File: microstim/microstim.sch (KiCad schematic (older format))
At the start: 81 parts

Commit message: tons of updates - beginning of layout as well.
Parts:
- removed BT?: 9V, symbol Device:Battery_Cell
- removed C? (x2): 1uF, symbol Device:C_Small
- removed U?: MCP3002, symbol Analog_ADC:MCP3002
- removed U?: L79L05_SO8, Package_SO:SOIC-8_3.9x4.9mm_P1.27mm, symbol Regulator_Linear:L79L05_SO8
- removed U? (x2): FQP47P06, symbol natecermak:FQP47P06
- removed U?: DG4053, symbol natecermak:DG4053
- added C11, C13, C16, C17, C37, C38, C39, C41, C5: 0.1uF, Capacitor_SMD:C_0603_1608Metric, symbol Device:C_Small
- added C28, C29: 100pF, Capacitor_SMD:C_0603_1608Metric, symbol Device:C_Small
- added C42: 680nF, Capacitor_SMD:C_0603_1608Metric, symbol Device:C_Small
- added R13, R14: 1k, Resistor_SMD:R_0603_1608Metric, symbol Device:R_US
- added RV4: 1k, Potentiometer_THT:Potentiometer_Bourns_3296Y_Vertical, symbol Device:R_POT
- added U10: AD7321, Package_SO:TSSOP-14_4.4x5mm_P0.65mm, symbol natecermak:AD7321
- added U17: LM358, Package_SO:SOIC-8_3.9x4.9mm_P1.27mm, symbol Amplifier_Operational:LM358
- added U18, U19: DG509ACWE, Package_SO:SOIC-16_3.9x9.9mm_P1.27mm, symbol natecermak:DG509ACWE
- added U7: ISO7341C, Package_SO:SOIC-16W_7.5x10.3mm_P1.27mm, symbol Isolator:ISO7341C
- C1, C10, C12, C14, C15, C18, C19, C2, C20, C21, C22, C23, C24, C25, C26, C27, C3, C30, C31, C32, C33, C34, C35, C36, C4, C40, C6, C7, C8, C9: renamed from C?; footprint (none) -> Capacitor_SMD:C_0603_1608Metric
- J1, J10, J12, J2, J5, J6: renamed from J?; footprint (none) -> Connector_Coaxial:SMA_Amphenol_901-144_Vertical
- J11: renamed from J?; footprint (none) -> TerminalBlock_4Ucon:TerminalBlock_4Ucon_1x02_P3.50mm_Horizontal
- J3, J4, J7, J8, J9: renamed from J?; footprint (none) -> TerminalBlock_4Ucon:TerminalBlock_4Ucon_1x02_P3.50mm_Vertical
- R1, R10, R11, R12, R2, R3, R4, R5, R6, R7, R8, R9: renamed from R?; footprint (none) -> Resistor_SMD:R_0603_1608Metric
- RV1, RV2, RV3: renamed from RV?; footprint (none) -> Potentiometer_THT:Potentiometer_Bourns_3296Y_Vertical
- SW1, SW2: renamed from SW?; footprint (none) -> Button_Switch_THT:SW_PUSH_6mm
- U1: renamed from U?; footprint (none) -> microstim:Teensy35_36
- U11, U12: renamed from U?; footprint (none) -> Package_SO:SOIC-8-N7_3.9x4.9mm_P1.27mm
- U13, U14: renamed from U?; footprint 21-0042B_16 -> Package_SO:SOIC-16_3.9x9.9mm_P1.27mm
- U15, U16: renamed from U?; footprint (none) -> Package_SO:SOIC-8_3.9x4.9mm_P1.27mm
- U2: renamed from U?; footprint (none) -> microstim:CC3-0512DF-E
- U9: renamed from U?; footprint (none) -> Package_SO:SOIC-14_3.9x8.7mm_P1.27mm
- gave numbers to parts that had none: 5
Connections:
- net labels added: CS2, CS2i, ISENSE0, ISENSE1, MISO2, MISO2i, MOSI2, MOSI2i, SCK2, SCK2i
- net labels removed: -5V, VIN_TEENSY
- wire segments 384 -> 497
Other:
- moved on the sheet: C1, C10, C12, C14, C15, C18, C19, C2, C20, C21, C22, C23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

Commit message: first complete draft of microstim PCB. no errors in layout.
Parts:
- removed U11, U12: LTC2057, Package_SO:SOIC-8-N7_3.9x4.9mm_P1.27mm, symbol natecermak:LTC2057
- added U11, U12: LTC2057, Package_SO:SOIC-8_3.9x4.9mm_P1.27mm, symbol Linear_Technology:LTC2057
- J11: footprint TerminalBlock_4Ucon:TerminalBlock_4Ucon_1x02_P3.50mm_Horizontal -> TerminalBlock_4Ucon:TerminalBlock_4Ucon_1x02_P3.50mm_Vertical
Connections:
- wire segments 497 -> 504
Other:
- moved on the sheet: RV1, RV4, SW1, SW2

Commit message: fixed some op-amps inserted backwards. also had to recommit everything due to OS upgrade and HD backup.
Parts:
- removed U11, U12: LTC2057, Package_SO:SOIC-8_3.9x4.9mm_P1.27mm, symbol Linear_Technology:LTC2057
- added U11, U12: LTC2057, Package_SO:SOIC-8-N7_3.9x4.9mm_P1.27mm, symbol natecermak:LTC2057
- C1: footprint Capacitor_SMD:C_0603_1608Metric -> Capacitor_SMD:C_1206_3216Metric_Pad1.42x1.75mm_HandSolder
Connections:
- wire segments 504 -> 509
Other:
- moved on the sheet: C21, C23, C26

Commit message: redesign based on improved howland source at jon newmans suggestion
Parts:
- removed C10, C26, C27, C30, C32, C34, C35, C37, C38, C39, C4, C41: 0.1uF, Capacitor_SMD:C_0603_1608Metric, symbol Device:C_Small
- removed C28, C29: 100pF, Capacitor_SMD:C_0603_1608Metric, symbol Device:C_Small
- removed R10: 5.5k, Resistor_SMD:R_0603_1608Metric, symbol Device:R_US
- removed R11, R12: 50k, Resistor_SMD:R_0603_1608Metric, symbol Device:R_US
- removed R14: 1k, Resistor_SMD:R_0603_1608Metric, symbol Device:R_US
- removed RV2, RV3: 1k, Potentiometer_THT:Potentiometer_Bourns_3296Y_Vertical, symbol Device:R_POT
- removed U11, U12: LTC2057, Package_SO:SOIC-8-N7_3.9x4.9mm_P1.27mm, symbol natecermak:LTC2057
- removed U13, U14, U19: DG509ACWE, Package_SO:SOIC-16_3.9x9.9mm_P1.27mm, symbol natecermak:DG509ACWE
- removed U16: LT1167, Package_SO:SOIC-8_3.9x4.9mm_P1.27mm, symbol natecermak:LT1167
- removed U17: LM358, Package_SO:SOIC-8_3.9x4.9mm_P1.27mm, symbol Amplifier_Operational:LM358
- removed U6: ISO7760, Package_SO:SOIC-16W_7.5x10.3mm_P1.27mm, symbol natecermak:ISO7760
- added U11: LT6657AHMS8-2.5, Package_SO:MSOP-8_3x3mm_P0.65mm, symbol Reference_Voltage:LT6657AHMS8-2.5
- added U12, U13: AD8276, Package_SO:SOIC-8_3.9x4.9mm_P1.27mm, symbol Amplifier_Difference:AD8276
- added U14: LT1167, Package_SO:SOIC-8_3.9x4.9mm_P1.27mm, symbol natecermak:LT1167
- added U16: DG509ACWE, Package_SO:SOIC-16_3.9x9.9mm_P1.27mm, symbol natecermak:DG509ACWE
- R1, R2, R5: value 25k -> 3k
- R4: value 250 -> 3k
- R6: value 25k -> 250
- R7: value 1k -> 1.2k
- R8: value 5.5k -> 1.2k
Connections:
- net labels added: 2.5V
- net labels removed: GS0_0, GS0_0i, GS0_1, GS0_1i, GS1_0, GS1_0i, GS1_1, GS1_1i
- wire segments 509 -> 365
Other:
- note added: "Max current output (0ohm load) is 2.5V/3k = +- 833uA.\nCurrent resolution is 5V/4096/3k = 0.4uA\nMax voltage output (infinite load) is 40/43*12V = 11.16V"
- note added: "gain is Rsense*(1+49.4k/Rg) = 250*(1+49.4k/1.2k) = 10.5 mV/uA\nVoltage output range is thus +-833*0.0105 = +-8.7V\noutput needs to be within +-10V\n"
- moved on the sheet: C12, C14, C20, C21, C31, C33, C36, C40, J1, J10, J11, J12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

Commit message: lots of cleanup in file structure. nearly ready to order board v0.12. need to finish BOM and commit.
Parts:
- removed U11: LT6657AHMS8-2.5, Package_SO:MSOP-8_3x3mm_P0.65mm, symbol Reference_Voltage:LT6657AHMS8-2.5
- added C4: 1uF, Capacitor_SMD:C_0603_1608Metric, symbol Device:C_Small
- added U6: AD1582, Package_TO_SOT_SMD:SOT-23, symbol natecermak:AD1582
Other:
- moved on the sheet: C1, C11, C12, C13, C14, C15, C16, C17, C18, C19, C2, C20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

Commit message: replaced LT1167 with INA826 instrument amp. hopefully this wasn't a terrible decision.
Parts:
- removed U14, U15: LT1167, Package_SO:SOIC-8_3.9x4.9mm_P1.27mm, symbol natecermak:LT1167
- added U11, U14: INA826, Package_SO:SOIC-8_3.9x4.9mm_P1.27mm, symbol natecermak:INA826
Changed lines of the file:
@@
 	6550 3950 6350 3950
-$Comp
-L natecermak:LT1167 U15
-U 1 1 5B7A1A5B
-P 11400 1050
-F 0 "U15" H 11841 1081 50  0000 L CNN
-F 1 "LT1167" H 11841 1004 31  0000 L CNN
-F 2 "Package_SO:SOIC-8_3.9x4.9mm_P1.27mm" H 11200 700 50  0001 C CNN
-F 3 "" H 11200 700 50  0001 C CNN
-	1    11400 1050
-	1    0    0    -1
-$EndComp
 $Comp
 L Isolator:ISO7341C U7
@@
 ISENSE1
 $Comp
-L natecermak:LT1167 U14
-U 1 1 5C968179
-P 11400 3200
-F 0 "U14" H 11841 3231 50  0000 L CNN
-F 1 "LT1167" H 11841 3154 31  0000 L CNN
-F 2 "Package_SO:SOIC-8_3.9x4.9mm_P1.27mm" H 11200 2850 50  0001 C CNN
-F 3 "" H 11200 2850 50  0001 C CNN
-	1    11400 3200
-	1    0    0    -1
-$EndComp
-$Comp
 L Device:R_US R2
 U 1 1 5C968180
@@
 Connection ~ 6550 3550
 Connection ~ 7450 3750
+$Comp
+L natecermak:INA826 U11
+U 1 1 5BF2F57D
+P 11400 1050
+F 0 "U11" H 11841 1088 50  0000 L CNN
+F 1 "INA826" H 11841 1005 39  0000 L CNN
+F 2 "Package_SO:SOIC-8_3.9x4.9mm_P1.27mm" H 11200 700 50  0001 C CNN
+F 3 "" H 11200 700 50  0001 C CNN
+	1    11400 1050
+	1    0    0    -1
+$EndComp
+$Comp
+L natecermak:INA826 U14
+U 1 1 5BF2F667
+P 11400 3200
+F 0 "U14" H 11841 3238 50  0000 L CNN
+F 1 "INA826" H 11841 3155 39  0000 L CNN
+F 2 "Package_SO:SOIC-8_3.9x4.9mm_P1.27mm" H 11200 2850 50  0001 C CNN
+F 3 "" H 11200 2850 50  0001 C CNN
+	1    11400 3200
+	1    0    0    -1
+$EndComp
 $EndSCHEMATC

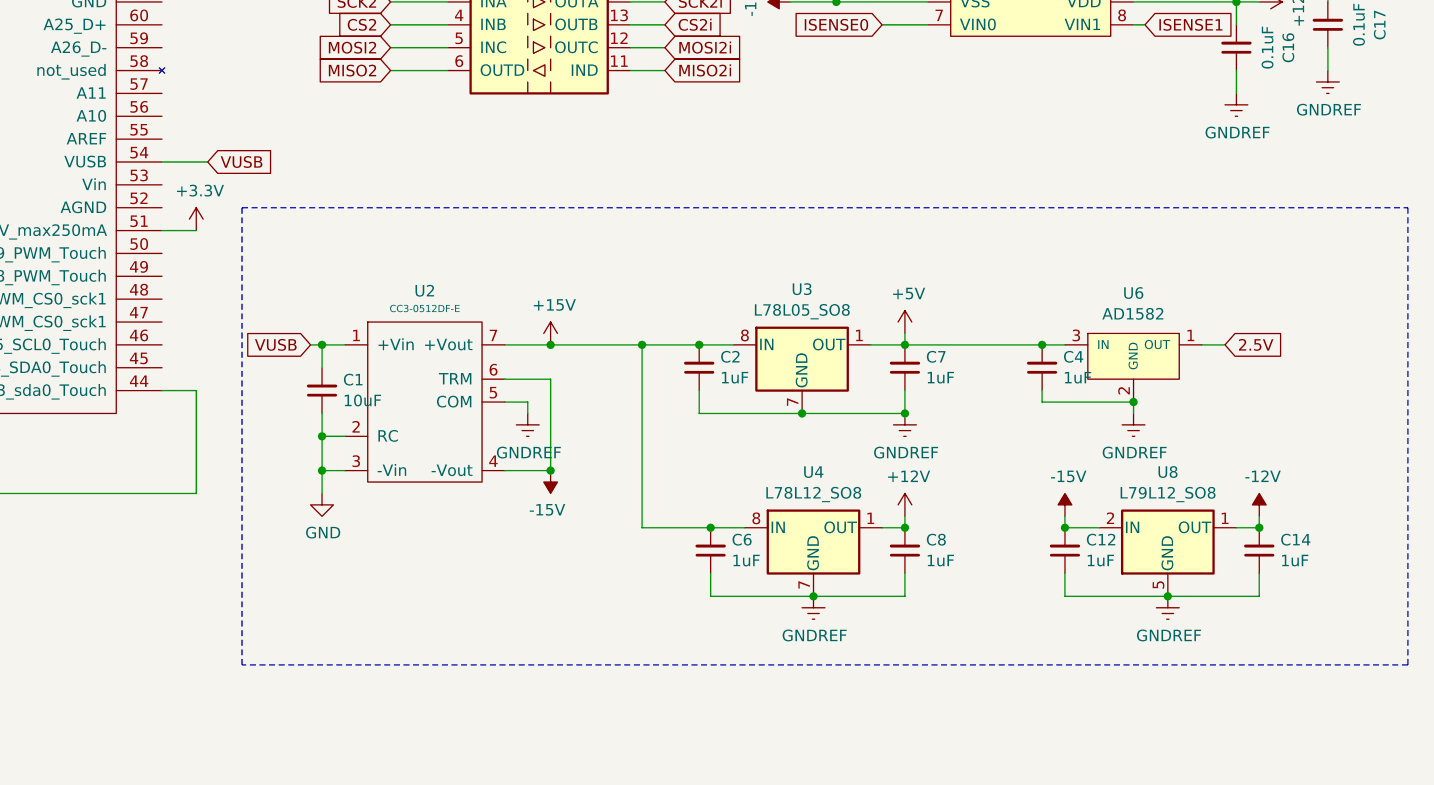
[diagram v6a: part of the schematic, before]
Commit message: bunch of small fixes to board. havent yet regenerated gerbers. also added beginnings of teensy controller code.
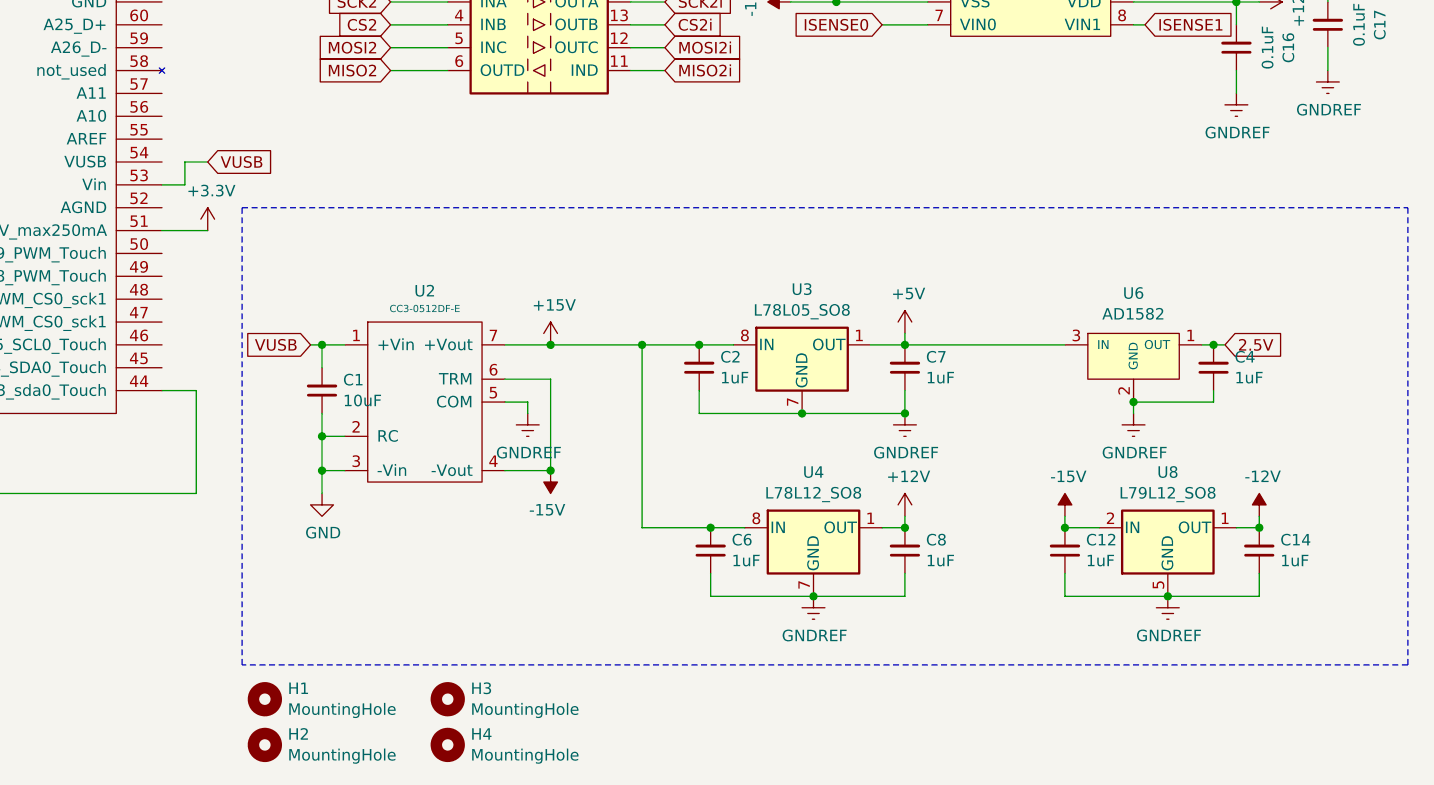
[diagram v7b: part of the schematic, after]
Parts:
- added H1, H2, H3, H4: MountingHole, MountingHole:MountingHole_5.3mm_M5, symbol Mechanical:MountingHole
- SW1, SW2: footprint Button_Switch_THT:SW_PUSH_6mm -> Button_Switch_SMD:SW_SPST_PTS645
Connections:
- net +5V: no longer C4.2
- net 2.5V: now also C4.2
- net VUSB: now also U1.53 (Vin); no longer U1.54 (VUSB)
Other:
- moved on the sheet: C4
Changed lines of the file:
@@
 F 0 "SW1" V 704 5698 50  0000 L CNN
 F 1 "SW_Push" V 795 5698 50  0000 L CNN
-F 2 "Button_Switch_THT:SW_PUSH_6mm" H 750 5750 50  0001 C CNN
+F 2 "Button_Switch_SMD:SW_SPST_PTS645" H 750 5750 50  0001 C CNN
 F 3 "" H 750 5750 50  0001 C CNN
 	1    750  5550
@@
 F 0 "SW2" V 904 5898 50  0000 L CNN
 F 1 "SW_Push" V 995 5898 50  0000 L CNN
-F 2 "Button_Switch_THT:SW_PUSH_6mm" H 950 5950 50  0001 C CNN
+F 2 "Button_Switch_SMD:SW_SPST_PTS645" H 950 5950 50  0001 C CNN
 F 3 "" H 950 5950 50  0001 C CNN
 	1    950  5750
@@
 Text GLabel 3400 4550 2    50   Input ~ 0
 VUSB
-Wire Wire Line
-	3400 4550 3200 4550
 $Comp
 L Device:C_Small C12
@@
 L power:+3.3V #PWR0103
 U 1 1 60B08A15
-P 3350 4850
-F 0 "#PWR0103" H 3350 4700 50  0001 C CNN
-F 1 "+3.3V" H 3365 5023 50  0000 C CNN
-F 2 "" H 3350 4850 50  0001 C CNN
-F 3 "" H 3350 4850 50  0001 C CNN
-	1    3350 4850
-	1    0    0    -1
-$EndComp
-Wire Wire Line
-	3200 4850 3350 4850
+P 3400 4850
+F 0 "#PWR0103" H 3400 4700 50  0001 C CNN
+F 1 "+3.3V" H 3415 5023 50  0000 C CNN
+F 2 "" H 3400 4850 50  0001 C CNN
+F 3 "" H 3400 4850 50  0001 C CNN
+	1    3400 4850
+	1    0    0    -1
+$EndComp
+Wire Wire Line
+	3200 4850 3400 4850
 $Comp
 L Device:R_US R1
@@
 	7450 5650 7450 5600
 Wire Wire Line
-	7750 5350 7850 5350
-Wire Wire Line
-	6450 5350 7050 5350
+	7750 5350 7800 5350
 $Comp
 L Device:C_Small C4
 U 1 1 5D09DD45
-P 7050 5450
-F 0 "C4" H 6958 5404 50  0000 R CNN
-F 1 "1uF" H 6958 5495 50  0000 R CNN
-F 2 "Capacitor_SMD:C_0603_1608Metric" H 7050 5450 50  0001 C CNN
-F 3 "~" H 7050 5450 50  0001 C CNN
-	1    7050 5450
-	-1   0    0    1
-$EndComp
-Connection ~ 7050 5350
-Wire Wire Line
-	7050 5350 7150 5350
-Wire Wire Line
-	7050 5550 7050 5600
-Wire Wire Line
-	7050 5600 7450 5600
-Connection ~ 7450 5600
+P 7800 5450
+F 0 "C4" H 7708 5404 50  0000 R CNN
+F 1 "1uF" H 7708 5495 50  0000 R CNN
+F 2 "Capacitor_SMD:C_0603_1608Metric" H 7800 5450 50  0001 C CNN
+F 3 "~" H 7800 5450 50  0001 C CNN
+	1    7800 5450
+	-1   0    0    1
+$EndComp
 Connection ~ 6550 3550
 Connection ~ 7450 3750
@@
 	1    0    0    -1
 $EndComp
+Wire Wire Line
+	3300 4550 3400 4550
+Wire Wire Line
+	3300 4650 3300 4550
+Wire Wire Line
+	3200 4650 3300 4650
+Connection ~ 7800 5350
+Wire Wire Line
+	7800 5350 7850 5350
+Wire Wire Line
+	6450 5350 7150 5350
+Wire Wire Line
+	7450 5600 7800 5600
+Wire Wire Line
+	7800 5600 7800 5550
+Connection ~ 7450 5600
+$Comp
+L Mechanical:MountingHole H1
+U 1 1 5C07145A
+P 3650 6900
+F 0 "H1" H 3750 6946 50  0000 L CNN
+F 1 "MountingHole" H 3750 6855 50  0000 L CNN
+F 2 "MountingHole:MountingHole_5.3mm_M5" H 3650 6900 50  0001 C CNN
+F 3 "~" H 3650 6900 50  0001 C CNN
+	1    3650 6900
+	1    0    0    -1
+$EndComp
+$Comp
+L Mechanical:MountingHole H2
+U 1 1 5C071952
+P 3650 7100
+F 0 "H2" H 3750 7146 50  0000 L CNN
+F 1 "MountingHole" H 3750 7055 50  0000 L CNN
+F 2 "MountingHole:MountingHole_5.3mm_M5" H 3650 7100 50  0001 C CNN
+F 3 "~" H 3650 7100 50  0001 C CNN
+	1    3650 7100
+	1    0    0    -1
+$EndComp
+$Comp
+L Mechanical:MountingHole H3
+U 1 1 5C071A16
+P 4450 6900
+F 0 "H3" H 4550 6946 50  0000 L CNN
+F 1 "MountingHole" H 4550 6855 50  0000 L CNN
+F 2 "MountingHole:MountingHole_5.3mm_M5" H 4450 6900 50  0001 C CNN
+F 3 "~" H 4450 6900 50  0001 C CNN
+	1    4450 6900
+	1    0    0    -1
+$EndComp
+$Comp
+L Mechanical:MountingHole H4
+U 1 1 5C071AE6
+P 4450 7100
+F 0 "H4" H 4550 7146 50  0000 L CNN
+F 1 "MountingHole" H 4550 7055 50  0000 L CNN
+F 2 "MountingHole:MountingHole_5.3mm_M5" H 4450 7100 50  0001 C CNN
+F 3 "~" H 4450 7100 50  0001 C CNN
+	1    4450 7100
+	1    0    0    -1
+$EndComp

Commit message: tons of changes - nearly done with pcb at 125x80mm (designed for slotted enclosure). now has 1) voltage output 2) voltage reading on ADC in both voltage output and current output modes. still need to redo BOM.
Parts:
- removed J2, J6: Conn_Coaxial, Connector_Coaxial:SMA_Amphenol_901-144_Vertical, symbol Connector:Conn_Coaxial
- removed J4, J8: Screw_Terminal_01x02, TerminalBlock_4Ucon:TerminalBlock_4Ucon_1x02_P3.50mm_Vertical, symbol Connector:Screw_Terminal_01x02
- removed RV1, RV4: 1k, Potentiometer_THT:Potentiometer_Bourns_3296Y_Vertical, symbol Device:R_POT
- added C10, C26: 10uF, Capacitor_SMD:C_1206_3216Metric_Pad1.42x1.75mm_HandSolder, symbol Device:C_Small
- added C27, C28, C29, C30, C32, C34: 0.1uF, Capacitor_SMD:C_0603_1608Metric, symbol Device:C_Small
- added R10, R12: 100, Resistor_SMD:R_0603_1608Metric, symbol Device:R_US
- added R11, R14: 180, Resistor_SMD:R_0603_1608Metric, symbol Device:R_US
- added R15, R16: 1k, Resistor_SMD:R_0603_1608Metric, symbol Device:R_US
- added R17, R18: 4k, Resistor_SMD:R_0603_1608Metric, symbol Device:R_US
- added U15, U17: OPA197, Package_SO:SOIC-8_3.9x4.9mm_P1.27mm, symbol natecermak:OPA197
- added U19, U20: DG419LDY, Package_SO:SOIC-8_3.9x4.9mm_P1.27mm, symbol Analog_Switch:DG419LDY
- H1, H2, H3, H4: footprint MountingHole:MountingHole_5.3mm_M5 -> MountingHole:MountingHole_4.3mm_M4
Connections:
- net +12V: now also C16.1, C27.2, C29.2, C34.2, U15.7 (V+), U17.7 (V+), U19.4 (V+), U20.4 (V+); no longer C16.2
- net +15V: now also C10.2
- net +5V: now also C17.1, R10.2, R12.2, U19.5 (VL), U20.5 (VL); no longer C17.2
- net -12V: now also C28.1, C30.1, C32.2, U15.4 (V-), U17.4 (V-), U19.7 (V-), U20.7 (V-)
- net -15V: now also C26.1
- net GNDREF: now also C16.2, C17.2, R9.1, U16.13 (S1B), U18.13 (S1B), C10.1, C26.2, C27.1, C28.2, C29.1, C30.2, C32.1, C34.1, R11.1, R14.1, U19.3 (GND), U20.3 (GND); no longer C16.1, C17.1, R9.2, U16.10 (S4B), U16.11 (S3B), U16.12 (S2B), U16.16 (A1), U18.10 (S4B), U18.11 (S3B), U18.12 (S2B), U18.16 (A1)
- net IOUT0: now also R3.2, U11.1 (-IN), U18.8 (DA); no longer J10.1 (In), J9.1 (Pin_1), U18.9 (DB)
- net IOUT1: now also R6.2, U14.1 (-IN), U16.8 (DA); no longer J11.1 (Pin_1), J12.1 (In), U16.9 (DB)
- net ISENSE0: now also U19.8; no longer U10.7 (VIN0)
- net ISENSE1: now also U20.8; no longer U10.8 (VIN1)
- net MOSI: now also U7.3 (INA); no longer U5.2 (INA)
- net MOSIi: now also U10.2 (DIN), U7.14 (OUTA); no longer U5.15 (OUTA)
- net NLDAC: now also U7.5 (INC); no longer U5.4 (INC)
- net NLDACi: now also U7.12 (OUTC); no longer U5.13 (OUTC)
- net OE0: now also U1.8 (6_PWM), U5.4 (INC); no longer U1.10 (8_TX3_miso0_sda0), U5.6 (INE)
- net OE0i: now also U5.13 (OUTC); no longer U5.11 (OUTE)
- net OE1: now also U1.7 (5_PWM_tx1_miso1), U5.5 (IND); no longer U1.9 (7_RX3_miso0_scl0), U5.7 (INF)
- net OE1i: now also U18.16 (A1), U5.12 (OUTD), U19.6; no longer U16.1 (A0), U5.10 (OUTF)
- net SCK0: now also U7.4 (INB); no longer U5.5 (IND)
- net SCK0i: now also U10.14 (SCLK), U7.13 (OUTB); no longer U5.12 (OUTD)
- net MISO: now reaches U1.14 (12_MISO0)
- net MISO: now also U7.6 (OUTD)
- net at U1.49 (22_A8_PWM_Touch): now also J1.1 (In), J3.1 (Pin_1)
- net OE3: now reaches U1.5 (3_PWM_CAN0TX_SCL2)
- net OE3: now also U5.7 (INF)
- net at U1.50 (23_A9_PWM_Touch): now also J5.1 (In), J7.1 (Pin_1)
- net OE2: now reaches U1.6 (4_PWM_CAN0RX_SDA2)
- net OE2: now also U5.6 (INE)
- net DAC1: now reaches R2.2, U9.10 (VB)
- net DAC1: now also U17.3 (+)
- net DAC0: now reaches R1.2, U9.14 (VA)
- net DAC0: now also U15.3 (+)
- net at U18.4 (S1A): now also R13.1, U18.6 (S3A); no longer U18.13 (S1B)
- net at U16.4 (S1A): now also R9.2, U16.6 (S3A); no longer U16.13 (S1B)
- net AIN0: no longer names the net of U1.32 (35_A16_PWM)
- net AIN1: no longer names the net of U1.31 (34_A15_CAN1TX_sda0)
- net CS2: no longer names the net of U1.23 (31_A12_RX4_CS1)
- net CS2: no longer U7.4 (INB)
- net CS2i renamed CS1i
- net CS1i: now also U5.14 (OUTB); no longer U7.13 (OUTB)
- net MISO2: no longer names the net of U1.3 (1_TX1_MISO1_Touch)
- net MISO2: no longer U7.6 (OUTD)
- net MISO2i renamed MISOi
- net MOSI2: no longer names the net of U1.2 (0_RX1_MOSI1_Touch)
- net MOSI2: no longer U7.5 (INC)
- removed net MOSI2i: U10.2 (DIN), U7.12 (OUTC)
- net SCK2: no longer names the net of U1.24 (32_A13_TX4_SCK1)
- net SCK2: no longer U7.3 (INA)
- removed net SCK2i: U10.14 (SCLK), U7.14 (OUTA)
- net SS: no longer names the net of U1.12 (10_PWM_TX2_CS0)
- net SS: no longer U5.3 (INB)
- net SSi renamed CS0i
- net CS0i: now also U5.15 (OUTA); no longer U5.14 (OUTB)
- removed net TRIG0: J1.1 (In), J3.1 (Pin_1), U1.30 (33_A14_CAN1TX_scl0)
- removed net TRIG1: J5.1 (In), J7.1 (Pin_1), U1.33 (36_A17_PWM)
- new net: U10.7 (VIN0), U19.1
- new net: U10.8 (VIN1), U20.1
- new net: U18.10 (S4B), U18.7 (S4A)
- new net: U18.12 (S2B), U18.5 (S2A)
- new net: R15.2, R17.1, U15.2 (-)
- new net: R10.1, R11.2, R15.1
- new net: R16.2, R18.1, U17.2 (-)
- new net: R12.1, R14.2, R16.1
- new net: U16.10 (S4B), U16.7 (S4A)
- new net: U16.12 (S2B), U16.5 (S2A)
- new net CS0: U1.10 (8_TX3_miso0_sda0), U5.2 (INA)
- new net CS1: U1.9 (7_RX3_miso0_scl0), U5.3 (INB)
- new net OE2i: U16.1 (A0), U5.11 (OUTE)
- new net OE3i: U16.16 (A1), U20.6, U5.10 (OUTF)
- new net OUT0: J10.1 (In), J9.1 (Pin_1), U18.9 (DB), U19.2
- new net OUT1: J11.1 (Pin_1), J12.1 (In), U16.9 (DB), U20.2
- new net VOUT0: R17.2, U15.6, U18.11 (S3B)
- new net VOUT1: R18.2, U16.11 (S3B), U17.6
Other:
- moved on the sheet: C1, C12, C13, C14, C15, C16, C17, C18, C19, C2, C20, C21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
